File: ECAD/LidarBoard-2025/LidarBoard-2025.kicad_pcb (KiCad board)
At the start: 2 copper layers, 68.8 x 76.2 mm, 45 parts, among them J1 Serial_Strategy, J2 Serial_Lidar, J3 Conn_01x03, J4 Oled, U1 Teensy3.2, U2 AMS1117-3.3

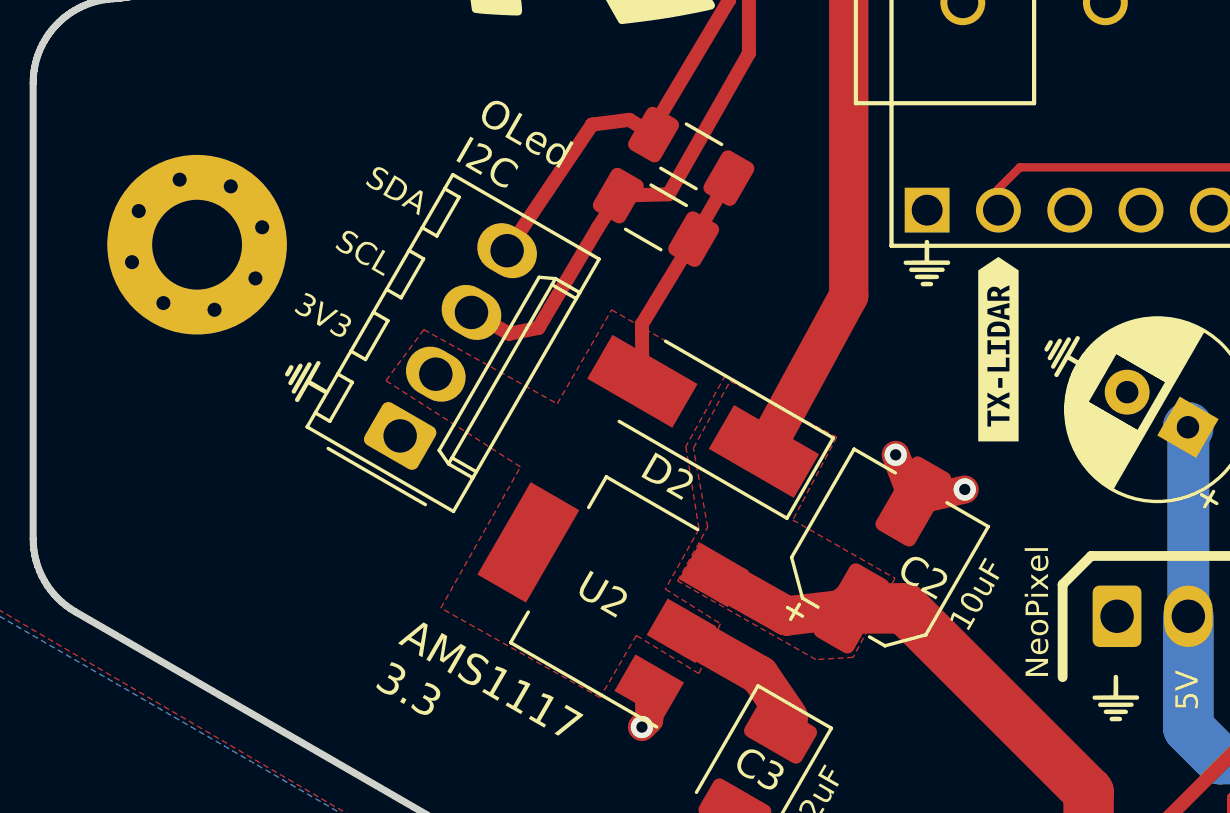
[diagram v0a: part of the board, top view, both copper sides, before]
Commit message: switch to KiCad 8 - Create Localisation version
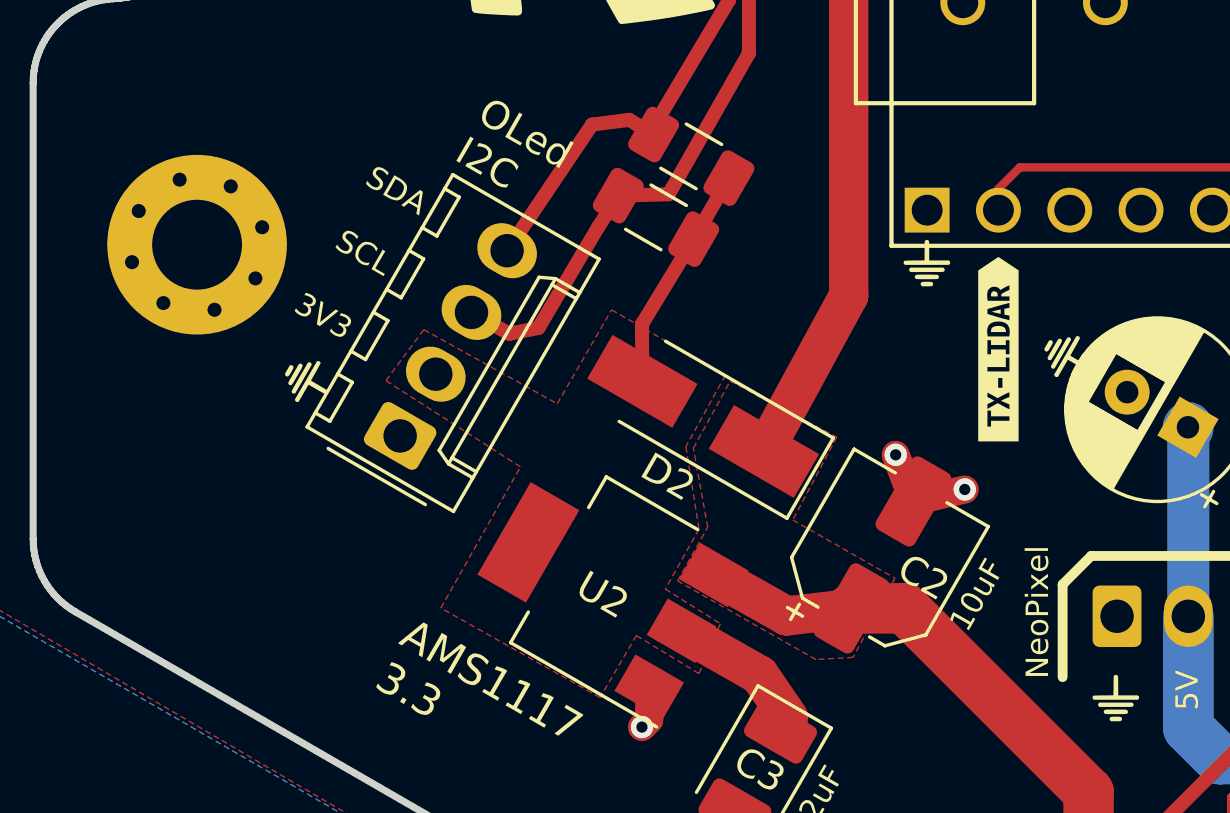
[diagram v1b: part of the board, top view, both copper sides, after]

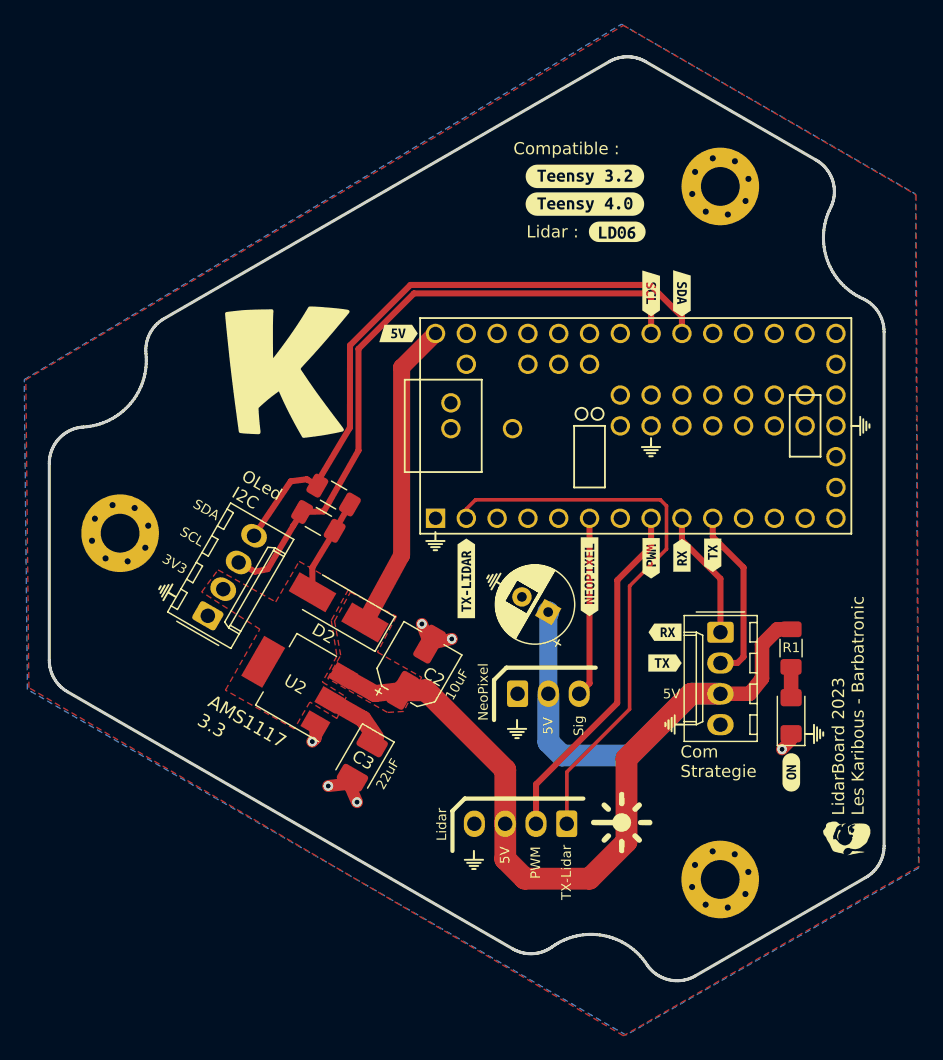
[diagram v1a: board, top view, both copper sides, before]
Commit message: add aisler logo
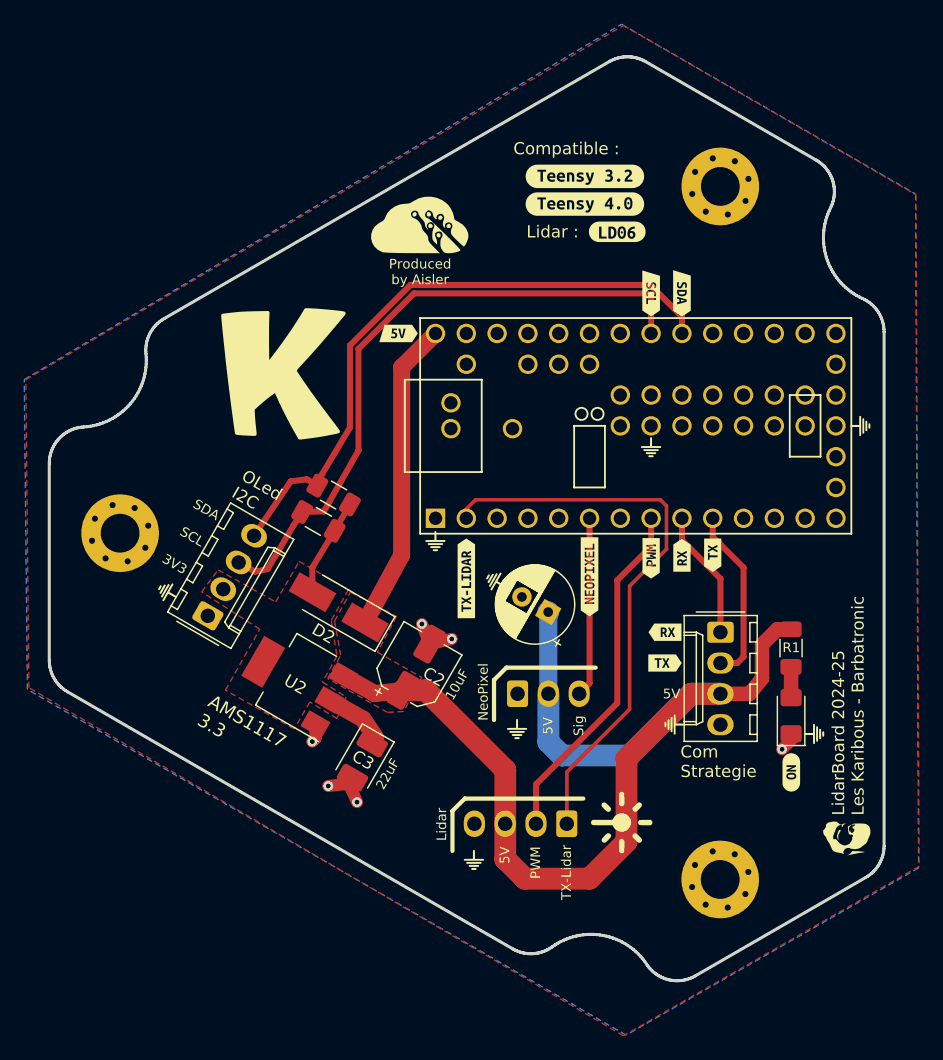
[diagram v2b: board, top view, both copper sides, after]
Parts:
- added G***: LOGO, LOGO, F.Cu at (138.4, 62.2)
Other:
- board text added: "LidarBoard 2024-25 Les Karibous - Barbatronic"
- board text added: "Produced by Aisler"
- board text removed: "LidarBoard 2023 Les Karibous - Barbatronic"
